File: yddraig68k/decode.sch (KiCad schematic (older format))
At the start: 31 parts, among them J401 NMI Reset, J402 Ext RUN LED, J403 Conn_01x06, Q401 2N4403, Q402 2N4403, Q403 2N4403, U401 74HC164, U402 74LS08, U403 74LS148, U404 XC95108PC84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

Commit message: Starting changes
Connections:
- net ~CPU_RESET: no longer U404.43 (P43)
- net ~HALT: no longer U404.41 (P41)
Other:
- moved on the sheet: D401, D402, D403, J402, J403, Q401, Q402, Q403, R402, R403, R404, R405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

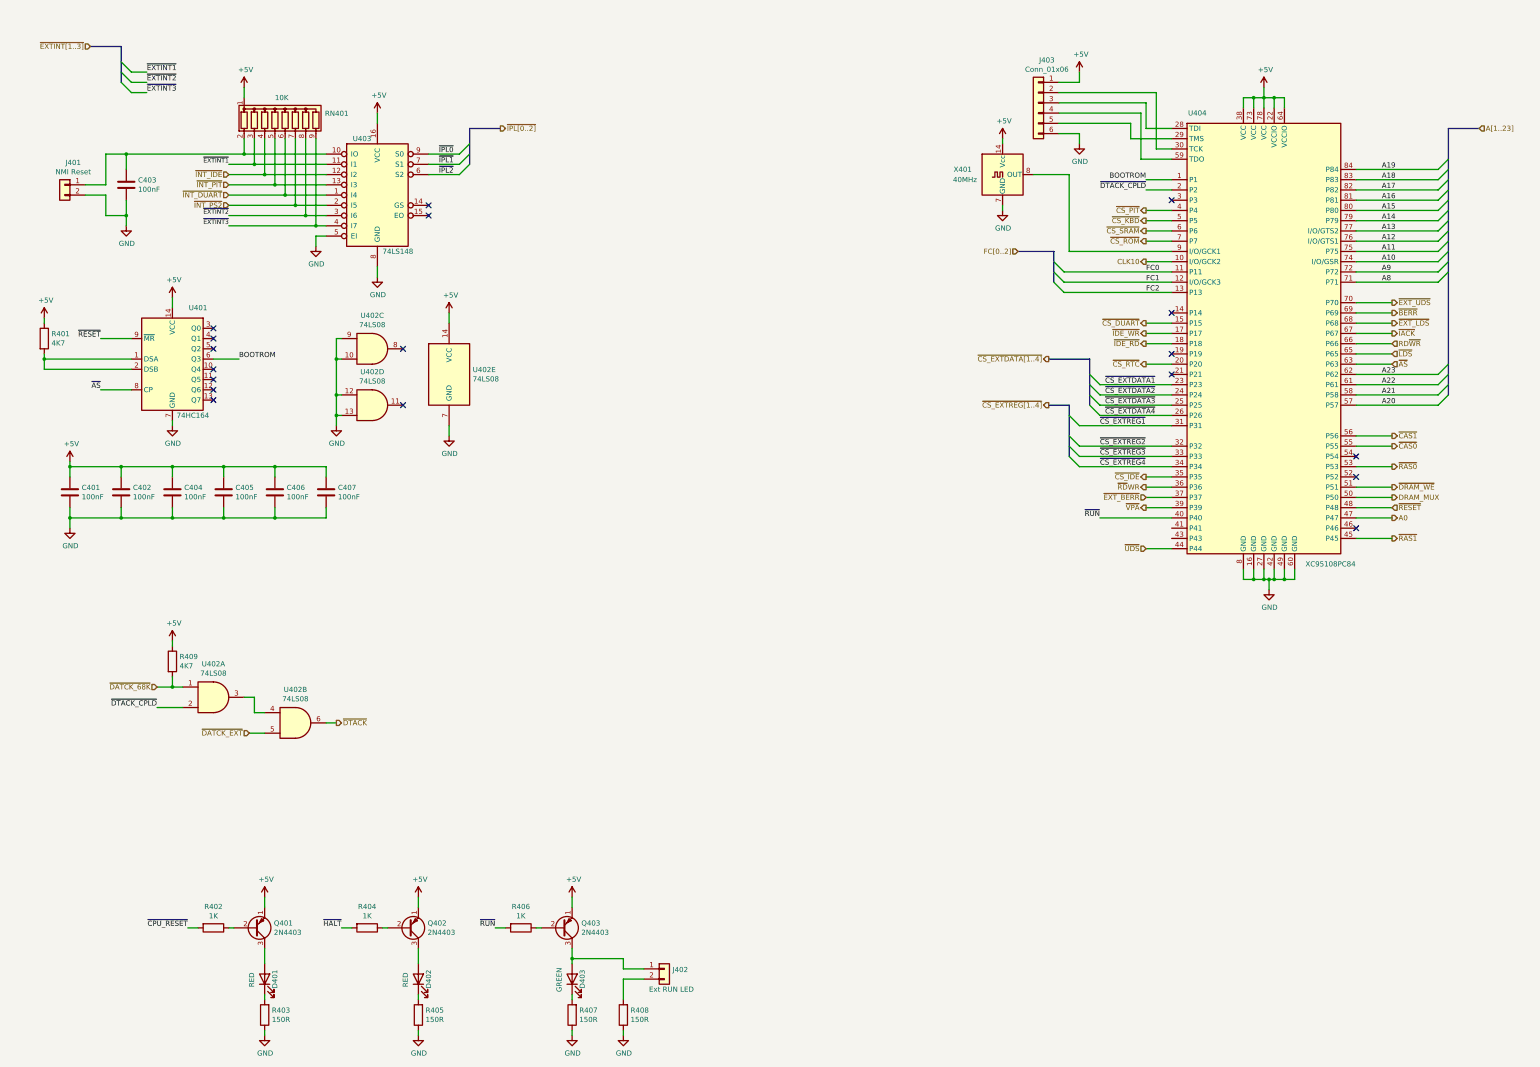
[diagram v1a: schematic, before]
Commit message: Changed schematic to more match proteus version
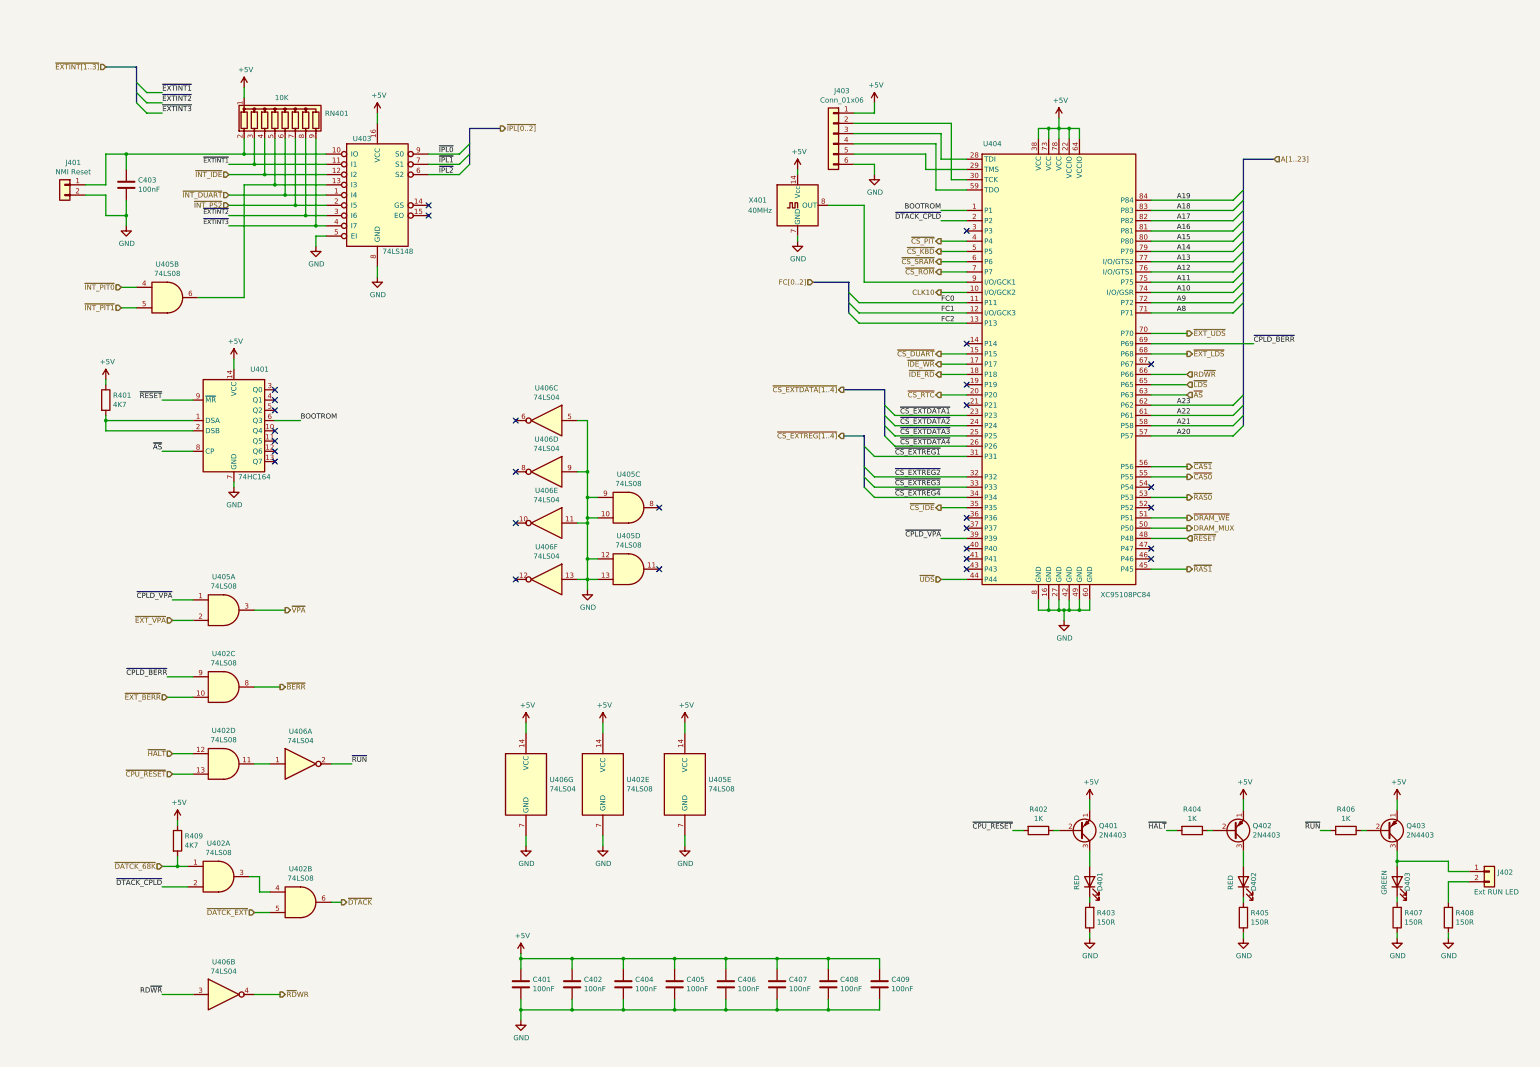
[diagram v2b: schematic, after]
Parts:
- added C408, C409: 100nF, Capacitor_THT:C_Disc_D3.8mm_W2.6mm_P2.50mm, symbol Device:C
- added U405: 74LS08, Package_DIP:DIP-14_W7.62mm_Socket, symbol 74xx:74LS08
- added U406: 74LS04, Package_DIP:DIP-14_W7.62mm_Socket, symbol 74xx:74LS04
- U402: footprint (none) -> Package_DIP:DIP-14_W7.62mm_Socket
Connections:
- net +5V: now also C408.1, C409.1, U405.14 (VCC), U406.14 (VCC)
- net GND: now also C408.2, C409.2, U405.10, U405.12, U405.13, U405.7 (GND), U405.9, U406.11, U406.13, U406.5, U406.7 (GND), U406.9; no longer U402.10, U402.12, U402.13, U402.9
- net RD~WR: now also U406.3
- net ~BERR: now also U402.8; no longer U404.69 (P69)
- net ~CPU_RESET: now also U402.13
- net ~EXT_BERR: now also U402.10; no longer U404.37 (P37)
- net ~HALT: now also U402.12
- net ~RD~WR: now also U406.4; no longer U404.36 (P36)
- net ~RUN: now also U406.2; no longer U404.40 (P40)
- net ~VPA: now also U405.3; no longer U404.39 (P39)
- net at U402.11: now also U406.1
- net A0: no longer names the net of U404.47 (P47)
- net ~IACK: no longer names the net of U404.67 (P67)
- net ~INT_PIT: no longer names the net of RN401.5 (R4), U403.13 (I3)
- net ~INT_PIT: now also U405.6
- new net ~CPLD_BERR: U402.9, U404.69 (P69)
- new net ~CPLD_VPA: U404.39 (P39), U405.1
- new net ~EXT_VPA: U405.2
- new net ~INT_PIT0: U405.4
- new net ~INT_PIT1: U405.5
- no-connect marks 18 -> 29
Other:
- moved on the sheet: C401, C402, C404, C405, C406, C407, D401, D402, D403, J402, J403, Q401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
